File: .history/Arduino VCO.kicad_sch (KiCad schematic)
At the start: 39 parts, among them U1 TL072

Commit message: renaming the global pins
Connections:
- net CV: no longer 68n3.2, D1.3 (K), J2.T, R4.2
- net Chord CV renamed CV 2
- net Chord/Wave renamed KNOB 3
- net Inversion renamed KNOB 2
- net Inversion CV renamed CV 3
- net Root Freq renamed KNOB 1
- new net CV 1: 68n3.2, D1.3 (K), J2.T, R4.2
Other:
- note added: "KNOB 1: FREQUENCY"
- note added: "KNOB 2: INVERSION"
- note added: "KNOB 3: CHORD/WAVE"
- note removed: "KNOB CHORD/WAVE"
- note removed: "KNOB ROOT: FREQUENCY"
- note removed: "KNOB: INVERSION"
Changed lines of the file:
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@@
 		)
 	)
-	(text "KNOB ROOT: FREQUENCY\n"
+	(text "KNOB 1: FREQUENCY\n"
 		(exclude_from_sim no)
 		(at 69.85 19.304 0)
@@
 		)
 	)
-	(text "KNOB CHORD/WAVE\n\n"
-		(exclude_from_sim no)
-		(at 80.01 112.522 0)
+	(text "KNOB 3: CHORD/WAVE\n\n"
+		(exclude_from_sim no)
+		(at 76.708 112.268 0)
 		(effects
 			(font
@@
 		)
 	)
-	(text "KNOB: INVERSION\n"
+	(text "KNOB 2: INVERSION\n"
 		(exclude_from_sim no)
 		(at 77.216 64.262 0)
@@
 		)
 	)
-	(global_label "Inversion CV"
+	(global_label "CV 3"
 		(shape input)
 		(at 161.29 132.08 0)
@@
 		)
 		(property "Intersheetrefs" "${INTERSHEET_REFS}"
-			(at 176.1285 132.08 0)
+			(at 168.8109 132.08 0)
 			(hide yes)
 			(show_name no)
@@
 		)
 	)
-	(global_label "Chord CV"
+	(global_label "CV 2"
 		(shape input)
 		(at 248.92 74.93 0)
@@
 		)
 		(property "Intersheetrefs" "${INTERSHEET_REFS}"
-			(at 260.7346 74.93 0)
+			(at 256.4409 74.93 0)
 			(hide yes)
 			(show_name no)
@@
 		)
 	)
-	(global_label "CV"
+	(global_label "CV 1"
 		(shape input)
 		(at 152.4 36.83 0)
@@
 		)
 		(property "Intersheetrefs" "${INTERSHEET_REFS}"
-			(at 157.7438 36.83 0)
+			(at 159.9209 36.83 0)
 			(hide yes)
 			(show_name no)
@@
 		)
 	)
-	(global_label "Inversion"
+	(global_label "KNOB 2"
 		(shape input)
 		(at 53.34 83.82 0)
@@
 		)
 		(property "Intersheetrefs" "${INTERSHEET_REFS}"
-			(at 64.8523 83.82 0)
+			(at 63.7033 83.82 0)
 			(hide yes)
 			(show_name no)
@@
 		)
 	)
-	(global_label "Chord CV"
+	(global_label "CV 2"
 		(shape input)
 		(at 161.29 85.09 0)
@@
 		)
 		(property "Intersheetrefs" "${INTERSHEET_REFS}"
-			(at 173.1046 85.09 0)
+			(at 168.8109 85.09 0)
 			(hide yes)
 			(show_name no)
@@
 		)
 	)
-	(global_label "Chord{slash}Wave"
+	(global_label "KNOB 3"
 		(shape input)
 		(at 248.92 69.85 0)
@@
 		)
 		(property "Intersheetrefs" "${INTERSHEET_REFS}"
-			(at 263.3955 69.85 0)
+			(at 259.2833 69.85 0)
 			(hide yes)
 			(show_name no)
@@
 		)
 	)
-	(global_label "Root Freq"
+	(global_label "KNOB 1"
 		(shape input)
 		(at 50.8 35.56 0)
@@
 		)
 		(property "Intersheetrefs" "${INTERSHEET_REFS}"
-			(at 63.1589 35.56 0)
+			(at 61.1633 35.56 0)
 			(hide yes)
 			(show_name no)
@@
 		)
 	)
-	(global_label "Chord{slash}Wave"
+	(global_label "KNOB 3"
 		(shape input)
 		(at 50.8 134.62 0)
@@
 		)
 		(property "Intersheetrefs" "${INTERSHEET_REFS}"
-			(at 65.2755 134.62 0)
+			(at 61.1633 134.62 0)
 			(hide yes)
 			(show_name no)
@@
 		)
 	)
-	(global_label "Inversion CV"
+	(global_label "CV 3"
 		(shape input)
 		(at 248.92 72.39 0)
@@
 		)
 		(property "Intersheetrefs" "${INTERSHEET_REFS}"
-			(at 263.7585 72.39 0)
+			(at 256.4409 72.39 0)
 			(hide yes)
 			(show_name no)
@@
 		)
 	)
-	(global_label "Root Freq"
+	(global_label "KNOB 1"
 		(shape input)
 		(at 248.92 62.23 0)
@@
 		)
 		(property "Intersheetrefs" "${INTERSHEET_REFS}"
-			(at 261.2789 62.23 0)
+			(at 259.2833 62.23 0)
 			(hide yes)
 			(show_name no)
@@
 		)
 	)
-	(global_label "Inversion"
+	(global_label "KNOB 2"
 		(shape input)
 		(at 248.92 64.77 0)
@@
 		)
 		(property "Intersheetrefs" "${INTERSHEET_REFS}"
-			(at 260.4323 64.77 0)
+			(at 259.2833 64.77 0)
 			(hide yes)
 			(show_name no)

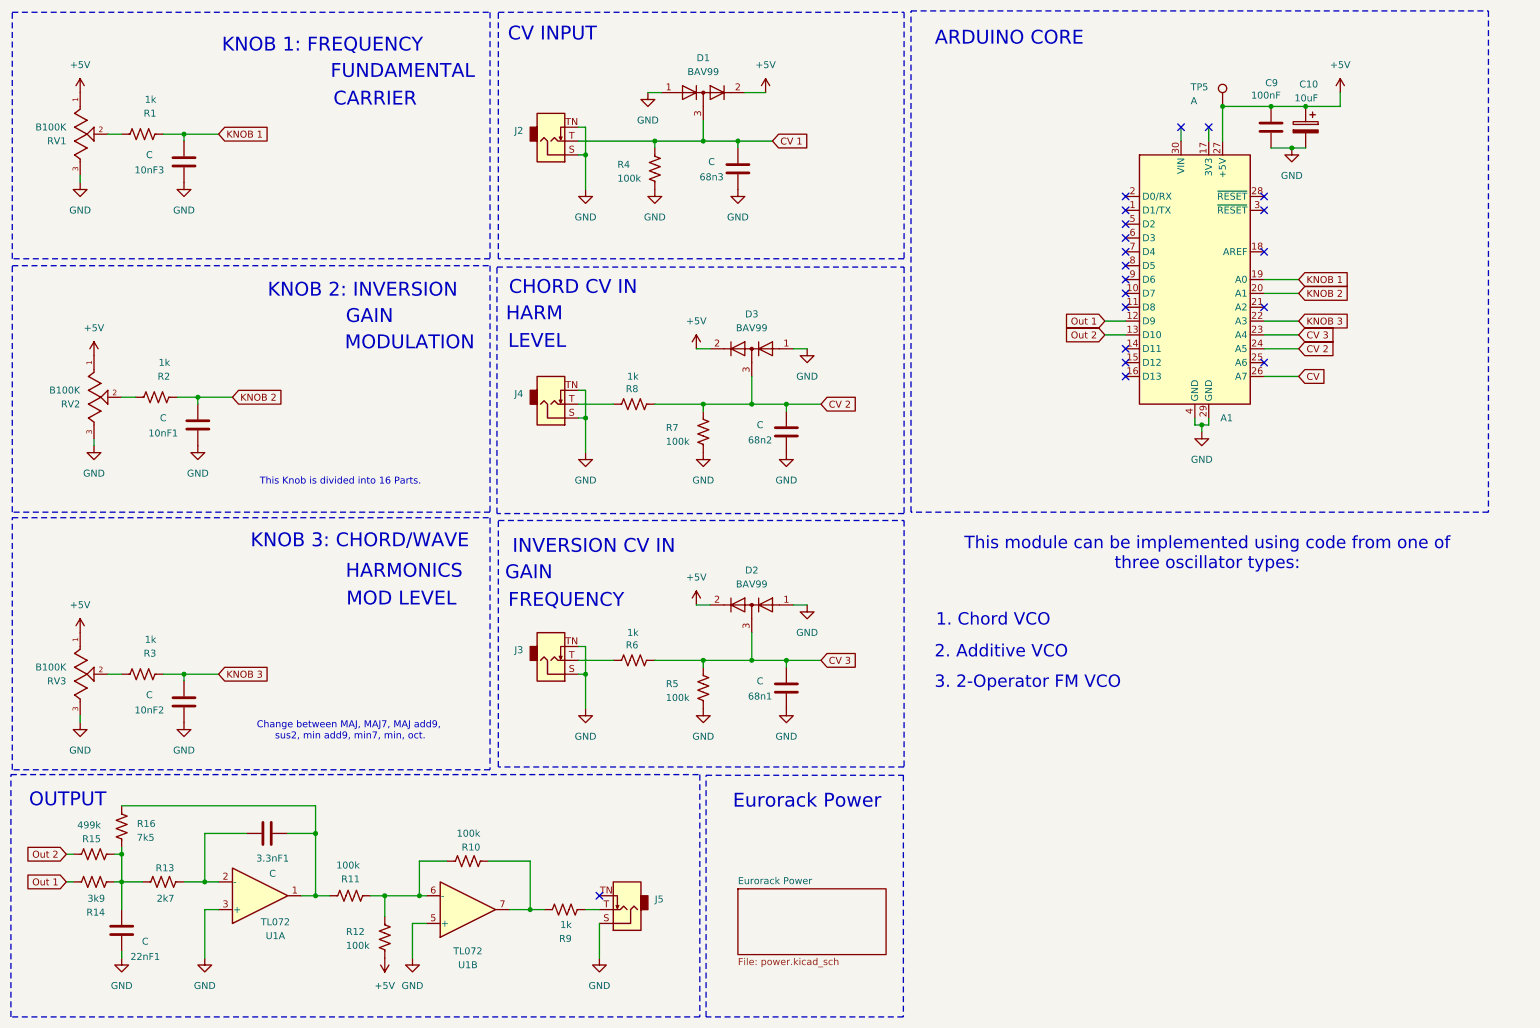
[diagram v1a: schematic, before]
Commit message: adding values to caps
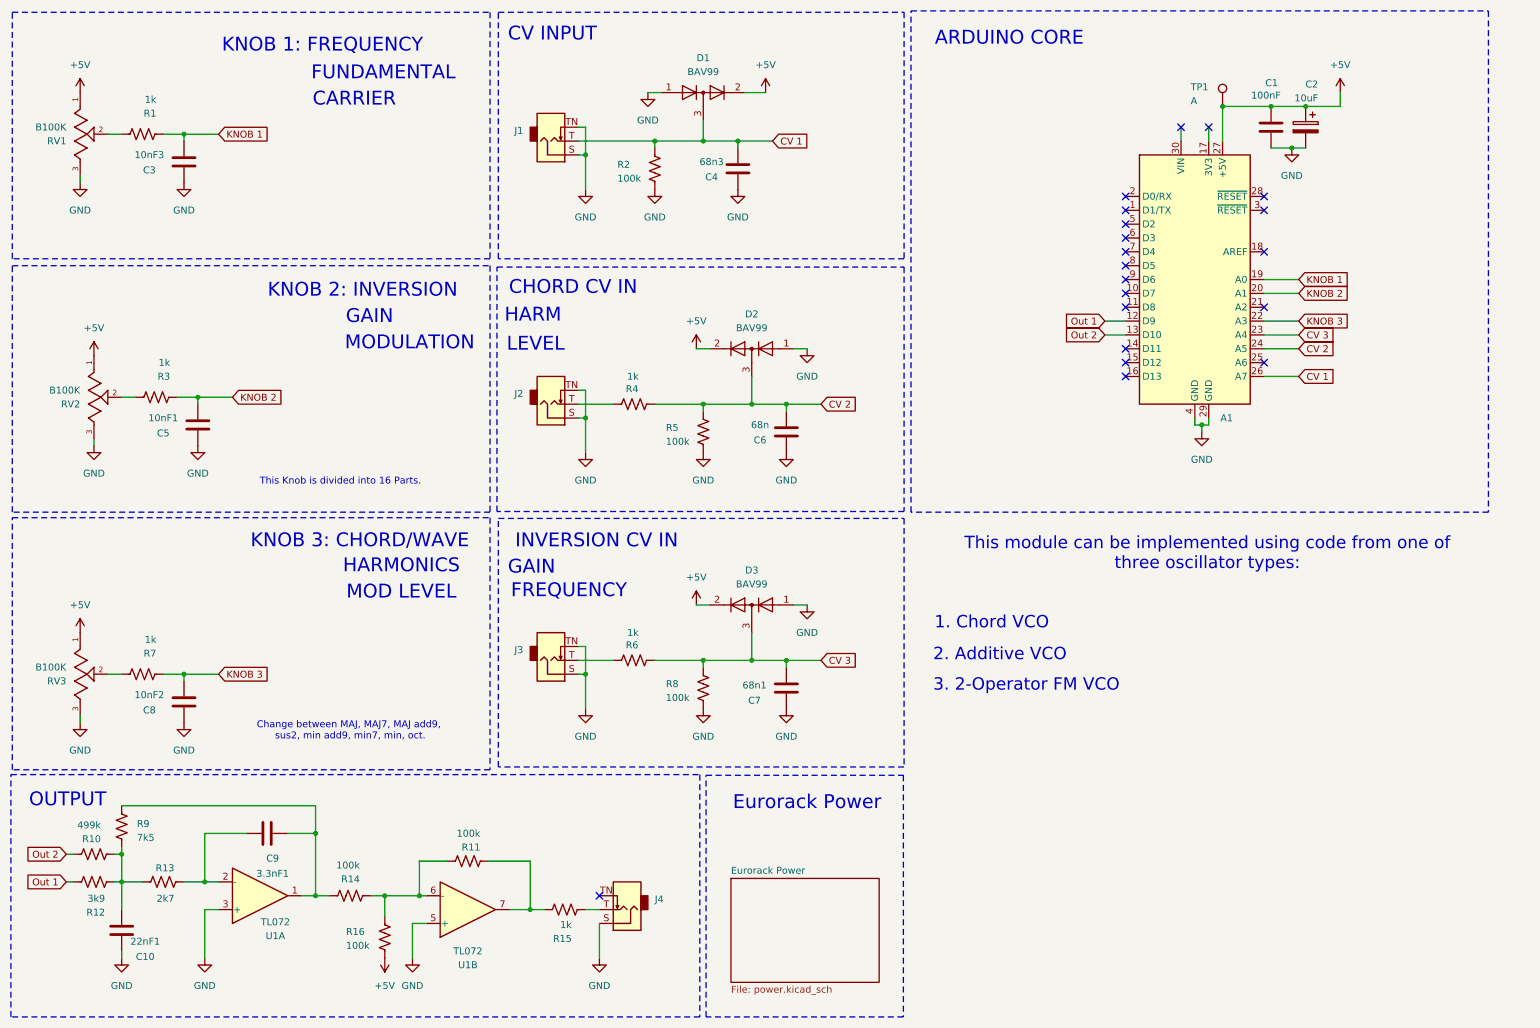
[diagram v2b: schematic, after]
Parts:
- C10: renamed from 22nF1; value C -> 22nF1; footprint (none) -> Capacitor_SMD:C_0805_2012Metric_Pad1.18x1.45mm_HandSolder
- C3: renamed from 10nF3; value C -> 10nF3; footprint (none) -> Capacitor_SMD:C_0805_2012Metric_Pad1.18x1.45mm_HandSolder
- C4: renamed from 68n3; value C -> 68n3; footprint (none) -> Capacitor_SMD:C_0805_2012Metric_Pad1.18x1.45mm_HandSolder
- C5: renamed from 10nF1; value C -> 10nF1; footprint (none) -> Capacitor_SMD:C_0805_2012Metric_Pad1.18x1.45mm_HandSolder
- C6: renamed from 68n2; value C -> 68n; footprint (none) -> Capacitor_SMD:C_0805_2012Metric_Pad1.18x1.45mm_HandSolder
- C7: renamed from 68n1; value C -> 68n1; footprint (none) -> Capacitor_SMD:C_0805_2012Metric_Pad1.18x1.45mm_HandSolder
- C8: renamed from 10nF2; value C -> 10nF2; footprint (none) -> Capacitor_SMD:C_0805_2012Metric_Pad1.18x1.45mm_HandSolder
- C9: renamed from 3.3nF1; value C -> 3.3nF1; footprint (none) -> Capacitor_SMD:C_0805_2012Metric_Pad1.18x1.45mm_HandSolder
- J1: renamed from J2; footprint (none) -> Eurorack:Jack_3.5mm_QingPu_WQP-PJ398SM_Vertical
- J2: renamed from J4; footprint (none) -> Eurorack:Jack_3.5mm_QingPu_WQP-PJ398SM_Vertical
- J3: footprint (none) -> Eurorack:Jack_3.5mm_QingPu_WQP-PJ398SM_Vertical
- J4: renamed from J5; footprint (none) -> Eurorack:Jack_3.5mm_QingPu_WQP-PJ398SM_Vertical
- R1, R13, R6: footprint (none) -> Resistor_SMD:R_0805_2012Metric_Pad1.20x1.40mm_HandSolder
- R10: renamed from R15; footprint (none) -> Resistor_SMD:R_0805_2012Metric_Pad1.20x1.40mm_HandSolder
- R11: renamed from R10; footprint (none) -> Resistor_SMD:R_0805_2012Metric_Pad1.20x1.40mm_HandSolder
- R12: renamed from R14; footprint (none) -> Resistor_SMD:R_0805_2012Metric_Pad1.20x1.40mm_HandSolder
- R14: renamed from R11; footprint (none) -> Resistor_SMD:R_0805_2012Metric_Pad1.20x1.40mm_HandSolder
- R15: renamed from R9; footprint (none) -> Resistor_SMD:R_0805_2012Metric_Pad1.20x1.40mm_HandSolder
- R16: renamed from R12; footprint (none) -> Resistor_SMD:R_0805_2012Metric_Pad1.20x1.40mm_HandSolder
- R2: renamed from R4; footprint (none) -> Resistor_SMD:R_0805_2012Metric_Pad1.20x1.40mm_HandSolder
- R3: renamed from R2; footprint (none) -> Resistor_SMD:R_0805_2012Metric_Pad1.20x1.40mm_HandSolder
- R4: renamed from R8; footprint (none) -> Resistor_SMD:R_0805_2012Metric_Pad1.20x1.40mm_HandSolder
- R5: renamed from R7; footprint (none) -> Resistor_SMD:R_0805_2012Metric_Pad1.20x1.40mm_HandSolder
- R7: renamed from R3; footprint (none) -> Resistor_SMD:R_0805_2012Metric_Pad1.20x1.40mm_HandSolder
- R8: renamed from R5; footprint (none) -> Resistor_SMD:R_0805_2012Metric_Pad1.20x1.40mm_HandSolder
- R9: renamed from R16; footprint (none) -> Resistor_SMD:R_0805_2012Metric_Pad1.20x1.40mm_HandSolder
- TP1: renamed from TP5; footprint (none) -> TestPoint:TestPoint_Pad_D1.5mm
- U1: footprint (none) -> Package_SO:SOIC-8_3.9x4.9mm_P1.27mm
- renumbered C9 to C1, C10 to C2, D3 to D2, D2 to D3
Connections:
- net CV is gone; now on net CV 1: A1.26 (A7)

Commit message: ordering the footprint nummeration
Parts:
- C10: value 22nF1 -> 22nF
- C3: value 10nF3 -> 10nF
- C4: value 68n3 -> 68n
- C5: value 10nF1 -> 10nF
- C7: value 68n1 -> 68n
- C8: value 10nF2 -> 10nF
- C9: value 3.3nF1 -> 3.3nF
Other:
- moved on the sheet: RV2
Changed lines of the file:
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@@
 	(wire
 		(pts
-			(xy 27.94 91.44) (xy 27.94 92.71)
+			(xy 148.59 80.01) (xy 148.59 85.09)
 		)
 		(stroke
@@
 	(wire
 		(pts
-			(xy 148.59 80.01) (xy 148.59 85.09)
+			(xy 31.75 92.71) (xy 27.94 92.71)
 		)
 		(stroke
@@
 	(wire
 		(pts
+			(xy 31.75 91.44) (xy 31.75 92.71)
+		)
+		(stroke
+			(width 0)
+			(type default)
+		)
+	)
+	(wire
+		(pts
 			(xy 139.7 133.35) (xy 139.7 132.08)
 		)
@@
 	(wire
 		(pts
+			(xy 31.75 76.2) (xy 27.94 76.2)
+		)
+		(stroke
+			(width 0)
+			(type default)
+		)
+	)
+	(wire
+		(pts
 			(xy 30.48 35.56) (xy 33.02 35.56)
 		)
@@
 	(wire
 		(pts
-			(xy 33.02 83.82) (xy 35.56 83.82)
-		)
-		(stroke
-			(width 0)
-			(type default)
-		)
-	)
-	(wire
-		(pts
 			(xy 154.94 133.35) (xy 154.94 132.08)
 		)
@@
 	(wire
 		(pts
+			(xy 36.83 83.82) (xy 35.56 83.82)
+		)
+		(stroke
+			(width 0)
+			(type default)
+		)
+	)
+	(wire
+		(pts
 			(xy 81.28 175.26) (xy 87.63 175.26)
 		)
@@
 			)
 		)
-		(property "Value" "10nF3"
+		(property "Value" "10nF"
 			(at 38.1 39.37 0)
 			(show_name no)
@@
 			)
 		)
-		(property "Value" "10nF2"
+		(property "Value" "10nF"
 			(at 38.1 138.43 0)
 			(show_name no)
@@
 			)
 		)
-		(property "Value" "22nF1"
+		(property "Value" "22nF"
 			(at 37.338 183.642 0)
 			(show_name no)
@@
 			)
 		)
-		(property "Value" "10nF1"
+		(property "Value" "10nF"
 			(at 40.64 87.63 0)
 			(show_name no)
@@
 	(symbol
 		(lib_id "Eurorack:Potentiometer_Alpha_RD901F_B100K_Vertical")
-		(at 27.94 83.82 90)
+		(at 31.75 83.82 90)
 		(mirror x)
 		(unit 1)
@@
 		(dnp no)
 		(property "Reference" "RV2"
-			(at 25.4 85.0901 90)
+			(at 29.21 85.0901 90)
 			(show_name no)
 			(do_not_autoplace no)
@@
 		)
 		(property "Value" "B100K"
-			(at 25.4 82.5501 90)
+			(at 29.21 82.5501 90)
 			(show_name no)
 			(do_not_autoplace no)
@@
 		)
 		(property "Footprint" "Eurorack:Potentiometer_Alpha_RD901F_Vertical_Alt"
-			(at 27.94 83.82 0)
+			(at 31.75 83.82 0)
 			(hide yes)
 			(show_name no)
@@
 		)
 		(property "Datasheet" ""
-			(at 27.94 83.82 0)
+			(at 31.75 83.82 0)
 			(hide yes)
 			(show_name no)
@@
 		)
 		(property "Description" ""
-			(at 27.94 83.82 0)
+			(at 31.75 83.82 0)
 			(hide yes)
 			(show_name no)
@@
 		)
 		(property "MF" "Alpha (Taiwan)"
-			(at 27.94 83.82 0)
+			(at 31.75 83.82 0)
 			(hide yes)
 			(show_name no)
@@
 		)
 		(property "MAXIMUM_PACKAGE_HEIGHT" "25.00 mm"
-			(at 27.94 83.82 0)
+			(at 31.75 83.82 0)
 			(hide yes)
 			(show_name no)
@@
 		)
 		(property "Package" "None"
-			(at 27.94 83.82 0)
+			(at 31.75 83.82 0)
 			(hide yes)
 			(show_name no)
@@
 		)
 		(property "Price" "None"
-			(at 27.94 83.82 0)
+			(at 31.75 83.82 0)
 			(hide yes)
 			(show_name no)
@@
 		)
 		(property "Check_prices" "https://www.snapeda.com/parts/RD901F-40-15R1-B100K-00DL1/Alpha/view-part/?ref=eda"
-			(at 27.94 83.82 0)
+			(at 31.75 83.82 0)
 			(hide yes)
 			(show_name no)
@@
 		)
 		(property "STANDARD" "Manufacturer recommendations"
-			(at 27.94 83.82 0)
+			(at 31.75 83.82 0)
 			(hide yes)
 			(show_name no)
@@
 		)
 		(property "PARTREV" "10/5/23"
-			(at 27.94 83.82 0)
+			(at 31.75 83.82 0)
 			(hide yes)
 			(show_name no)
@@
 		)
 		(property "SnapEDA_Link" "https://www.snapeda.com/parts/RD901F-40-15R1-B100K-00DL1/Alpha/view-part/?ref=snap"
-			(at 27.94 83.82 0)
+			(at 31.75 83.82 0)
 			(hide yes)
 			(show_name no)
@@
 		)
 		(property "MP" "RD901F-40-15R1-B100K-00DL1"
-			(at 27.94 83.82 0)
+			(at 31.75 83.82 0)
 			(hide yes)
 			(show_name no)
@@
 		)
 		(property "Description_1" "Potentiometers 9mm Linear 100K Round Shaft"
-			(at 27.94 83.82 0)
+			(at 31.75 83.82 0)
 			(hide yes)
 			(show_name no)
@@
 		)
 		(property "Availability" "Not in stock"
-			(at 27.94 83.82 0)
+			(at 31.75 83.82 0)
 			(hide yes)
 			(show_name no)
@@
 		)
 		(property "MANUFACTURER" "Alpha Taiwan"
-			(at 27.94 83.82 0)
+			(at 31.75 83.82 0)
 			(hide yes)
 			(show_name no)
@@
 			)
 		)
-		(property "Value" "68n3"
+		(property "Value" "68n"
 			(at 141.224 40.64 0)
 			(show_name no)
@@
 			)
 		)
-		(property "Value" "3.3nF1"
+		(property "Value" "3.3nF"
 			(at 60.706 171.196 90)
 			(show_name no)
@@
 			)
 		)
-		(property "Value" "68n1"
+		(property "Value" "68n"
 			(at 149.098 136.652 0)
 			(show_name no)
